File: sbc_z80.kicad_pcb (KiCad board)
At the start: 4 copper layers, 102.6 x 50.8 mm, 95 parts, among them J1 RC80 Bus, J2 CTC Header, J3 AVR-JTAG-10, J4 IDE, J5 PIO Header, J6 Port A, J7 Port B, J8 USB_B_Micro, Q1 IRLML6402, SW1 Reset, U1 DS1813R-5+T&R, U10 Z84C2010AEG, U11 74HCT273, U12 MAX40200AUK, U2 AP7381-33SA, U3 CPU -Z84C0020AEG, U4 CTC - Z84C3010AEG, U5 CPLD - EPM7032STC44, U6 SRAM - IS62C5128BL-45TLI, U7 74HCT2G04, U8 SST39SF040, U9 SIO/3 - Z84C4310AEG, X1 CTX-636 50mhz

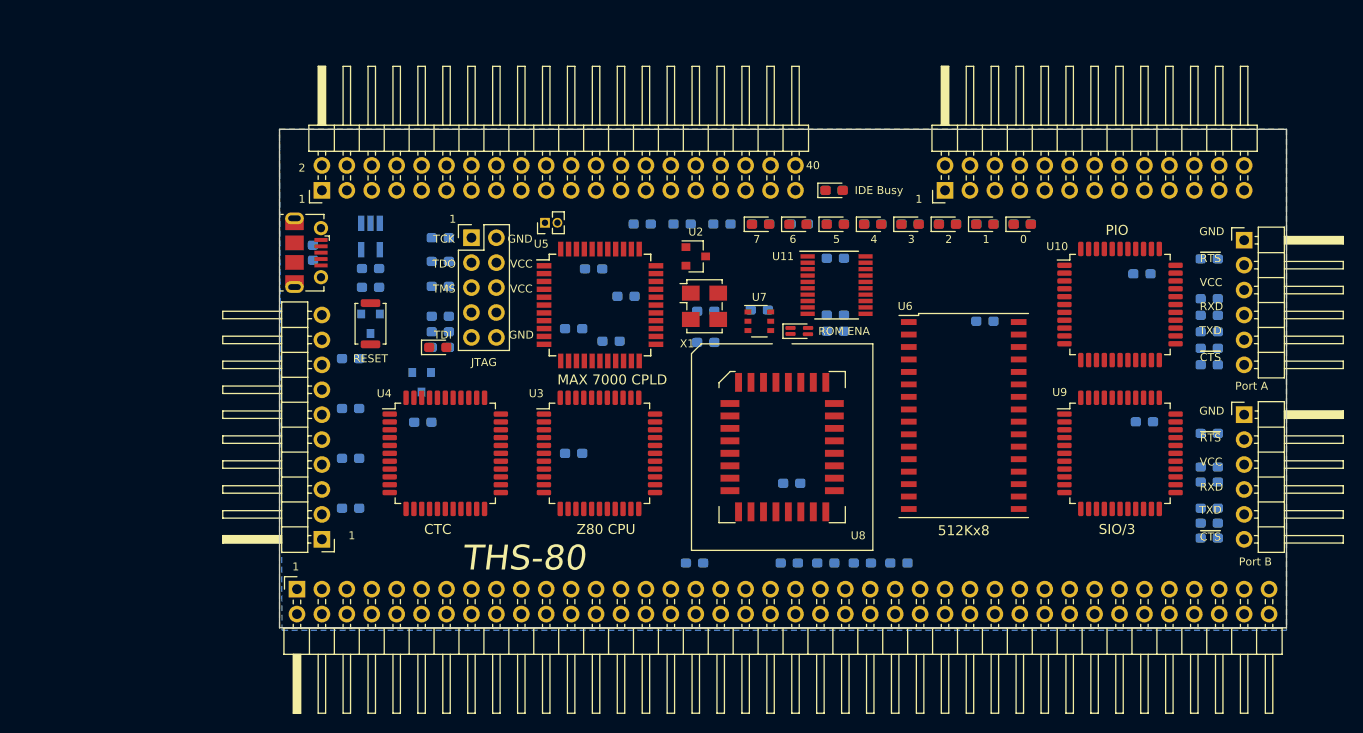
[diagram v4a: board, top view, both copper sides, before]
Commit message: address lines routed
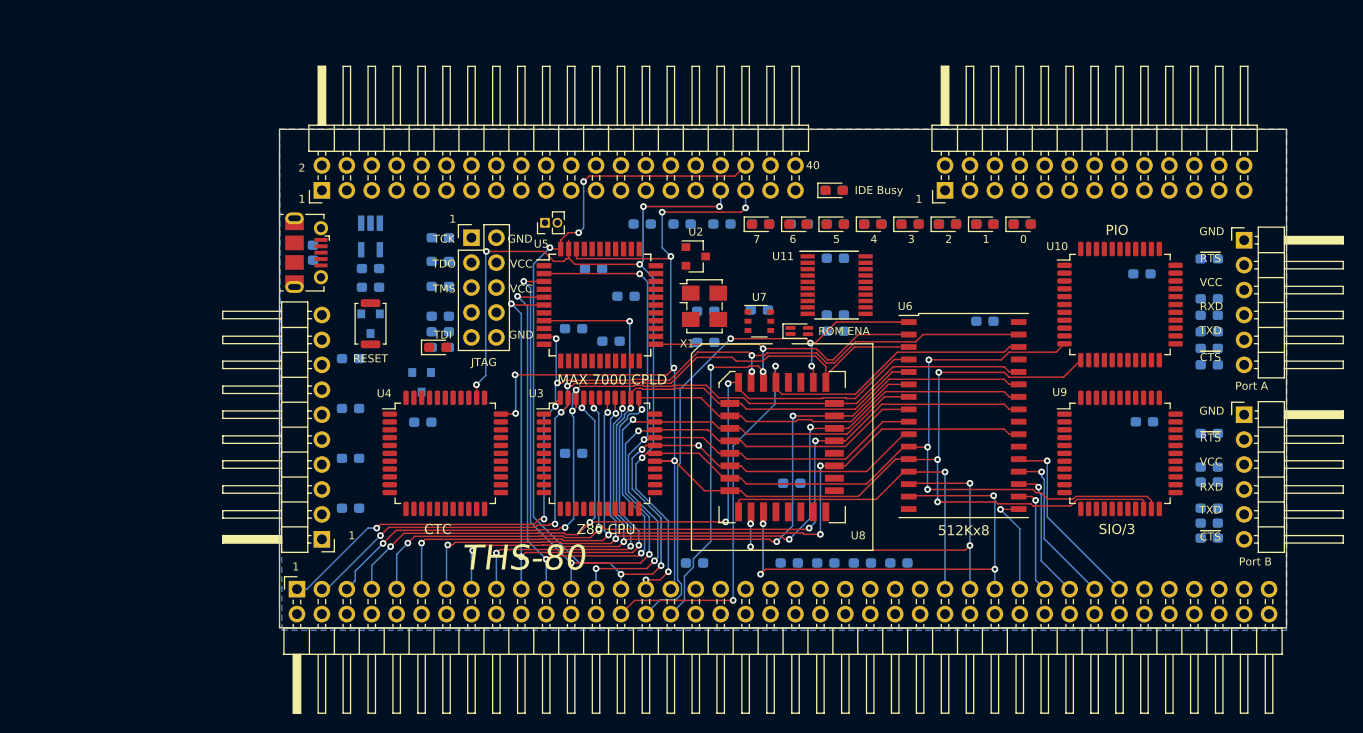
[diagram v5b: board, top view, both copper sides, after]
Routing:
- net /A1: track 0.00 -> 170.3 mm, vias 0 -> 11
- net /A0: track 0.00 -> 166.5 mm, vias 0 -> 10
- net /A2: track 0.00 -> 115.8 mm, vias 0 -> 7
- net /A15: track 0.00 -> 102.6 mm, vias 0 -> 7
- net /A6: track 0.00 -> 93.2 mm, vias 0 -> 4
- net /A11: track 0.00 -> 91.8 mm, vias 0 -> 5
- net /A9: track 0.00 -> 90.2 mm, vias 0 -> 5
- net /A12: track 0.00 -> 89.7 mm, vias 0 -> 5
- net /A8: track 0.00 -> 89.4 mm, vias 0 -> 5
- net /A13: track 0.00 -> 89.4 mm, vias 0 -> 4
- net /A10: track 0.00 -> 89.2 mm, vias 0 -> 5
- net /A5: track 0.00 -> 89.1 mm, vias 0 -> 4
- net /A4: track 0.00 -> 87.6 mm, vias 0 -> 4
- net /A7: track 0.00 -> 83.2 mm, vias 0 -> 4
- net /A14: track 0.00 -> 81.8 mm, vias 0 -> 4
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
